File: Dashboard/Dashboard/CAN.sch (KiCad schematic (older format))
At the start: 23 parts, among them J4 CAN_Out, U4 ADM3055E, U5 CDSOT23-T24CAN

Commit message: Make major changes to Dashboard and file structure.
Problem
=======
* The dashboard needs to be redesigned. These are continuing changes
to Dashboard 2.0.
* There are way too many files cluttering the Dashboard folder.
* We need to include LED indicators for the driver that make sense.

Solution
========
* I made major changes to the dashboard. These include the following:
  * Add an external LED board to mount on the steering wheel.
  * Add hardware timer circuitry for lights, so that the software does
    not have to concern itself with the flashers.
  * Generally cleaned up the dashboard's schematics
* There have also been changes made to the file system. All extra files
  that were not necessary have been removed. In the future, reference
  materials should be kept outside of version control.

Notes
=====
The dashboard still is not complete. We still need to address the following:
1. Pin assignments right now are mostly arbitrary. They are still subject to change.
2. The design needs to be verified.
3. We need to settle on the interface. Things like the ignition dial are still
   possible to change if we desire.
4. We need to add another potentiometer for the accelerator. This is missing because
   it was previously handled by the motor interface board.
5. Probably some other things that I'm forgetting.
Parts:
- removed J4: CAN_Out, UTSVT_Connectors:Molex_MicroFit3.0_1x4xP3.00mm_PolarizingPeg_Vertical, symbol utsvt-connectors:CANConnector
- removed TP6: CAN_ISO_Vout, TestPoint:TestPoint_Keystone_5005-5009_Compact, symbol Connector:TestPoint
- removed TP7: CAN_ISO_Vin, TestPoint:TestPoint_Keystone_5005-5009_Compact, symbol Connector:TestPoint
- removed TP8: CAN_ISO_GndIn, TestPoint:TestPoint_Keystone_5005-5009_Compact, symbol Connector:TestPoint
- removed TP9: CAN_ISO_GndOut, TestPoint:TestPoint_Keystone_5005-5009_Compact, symbol Connector:TestPoint
- removed U4: ADM3055E, UTSVT_ICs:SOIC-20W_7.5x15.4mm_Pitch1.27mm, symbol utsvt-chips:ADM3055E
- removed U5: CDSOT23-T24CAN, Package_TO_SOT_SMD:SOT-23W, symbol utsvt-chips:CDSOT23-T24CAN
- added J201: CAN_IN, utsvt_conn:Molex_MicroFit3.0_1x4xP3.00mm_PolarizingPeg_Vertical, symbol Connector_Generic:Conn_01x04
- added J202: CAN_OUT, utsvt_conn:Molex_MicroFit3.0_1x4xP3.00mm_PolarizingPeg_Vertical, symbol Connector_Generic:Conn_01x04
- added U201: ADM3055E, utsvt_ics:SOIC-20W_7.5x15.4mm_Pitch1.27mm, symbol Chips:ADM3055E
- added U202: CDSOT23-T24CAN, Package_TO_SOT_SMD:SOT-23W, symbol Chips:CDSOT23-T24CAN
- C201: renamed from C18; Mouser Part Number (none) -> 80-C0805C106K8RAUTO
- C202: renamed from C19; Mouser Part Number (none) -> 80-C0805C104K3R
- C203: renamed from C20; Mouser Part Number (none) -> 80-C0805C104K3R
- C204: renamed from C21; Mouser Part Number (none) -> 80-C0805X103K1R3316
- C205: renamed from C22; value 10uF -> 0.22uF; Mouser Part Number (none) -> 80-C0805C224J1RECTU
- C206: renamed from C23; value 0.22uF -> 10uF; Mouser Part Number (none) -> 80-C0805C106K8RAUTO
- C207: renamed from C24; Mouser Part Number (none) -> 80-C0805C104K3R
- C208: renamed from C25; Mouser Part Number (none) -> 80-C0805X103K1R3316
- L201: renamed from L2; Mouser Part Number (none) -> 963-BK2125LM182-T
- L202: renamed from L3; Mouser Part Number (none) -> 963-BK2125LM182-T
- R201: renamed from R2; Mouser Part Number (none) -> 71-CRCW08050000Z0EAC
- R202: renamed from R3; Mouser Part Number (none) -> 71-CRCW080559R0FKEA
- R203: renamed from R4; Mouser Part Number (none) -> 71-CRCW080559R0FKEA
- renumbered JP1 to JP201, TP10 to TP201, TP11 to TP202
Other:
- note added: "As long as total equals to 120 Ohms,\nthe two termination resistors can be any value"

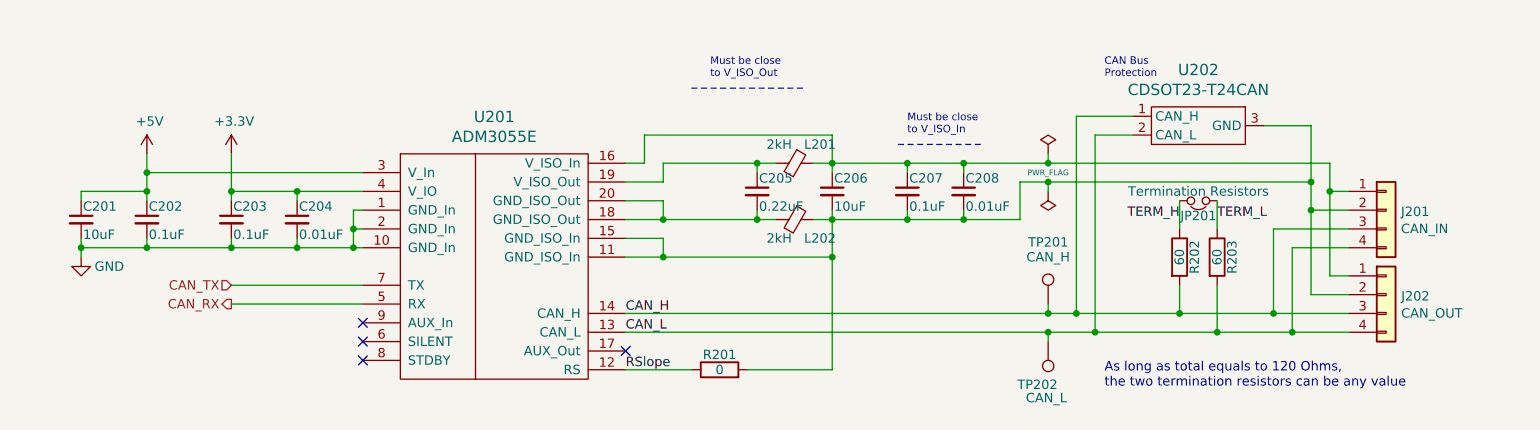
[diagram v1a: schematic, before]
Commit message: Change the MCU to the R (64-pin) variant.
Problem
=======
I don't want to have to solder 144 pins.

Solution
========
I changed the package of the MCU to the 64-pin
version, which now makes it the exact same as
the BPS.
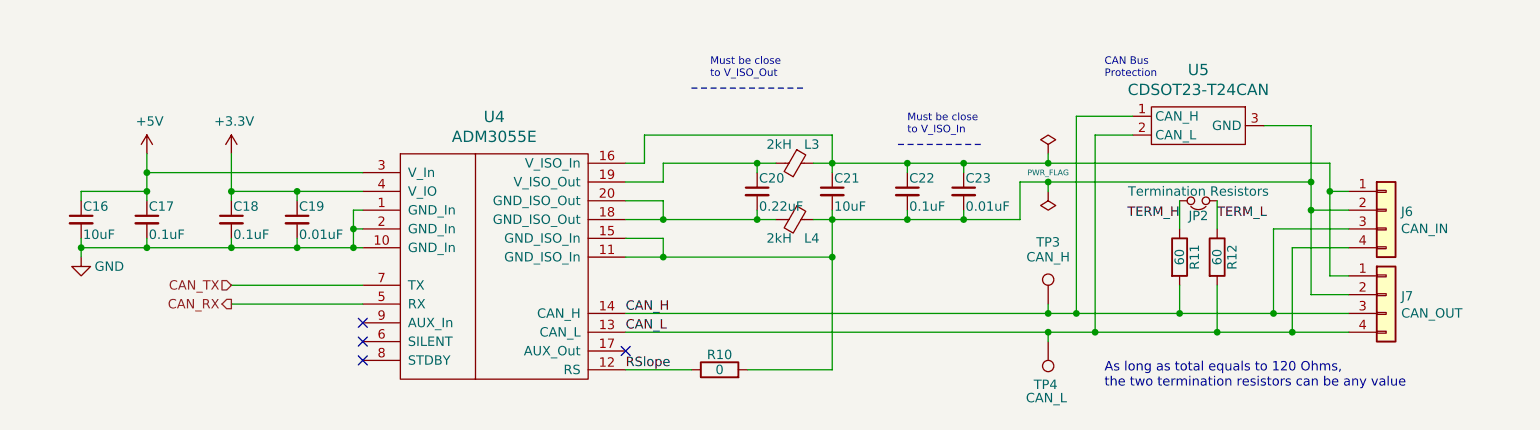
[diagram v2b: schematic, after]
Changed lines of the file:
@@
 $Descr A4 11693 8268
 encoding utf-8
-Sheet 2 6
+Sheet 5 6
 Title ""
 Date ""
@@
 AR Path="/5E80FF20/5C2B42FA" Ref="R?"  Part="1"
 AR Path="/5EA71171/5C2B42FA" Ref="R503"  Part="1"
-F 0 "R203" V 8280 3550 50  0000 C CNN
+AR Path="/5F479052/5C2B42FA" Ref="R9"  Part="1"
+AR Path="/5F547B94/5C2B42FA" Ref="R12"  Part="1"
+F 0 "R12" V 8280 3550 50  0000 C CNN
 F 1 "60" V 8200 3550 50  0000 C CNN
 F 2 "Resistor_SMD:R_0805_2012Metric" V 8130 3550 50  0001 C CNN
@@
 AR Path="/5E80FF20/5C2B4301" Ref="R?"  Part="1"
 AR Path="/5EA71171/5C2B4301" Ref="R502"  Part="1"
-F 0 "R202" V 8080 3550 50  0000 C CNN
+AR Path="/5F479052/5C2B4301" Ref="R8"  Part="1"
+AR Path="/5F547B94/5C2B4301" Ref="R11"  Part="1"
+F 0 "R11" V 8080 3550 50  0000 C CNN
 F 1 "60" V 8000 3550 50  0000 C CNN
 F 2 "Resistor_SMD:R_0805_2012Metric" V 7930 3550 50  0001 C CNN
@@
 AR Path="/5E80FF20/5C2B4308" Ref="JP?"  Part="1"
 AR Path="/5EA71171/5C2B4308" Ref="JP501"  Part="1"
-F 0 "JP201" H 8100 3330 50  0000 C CNN
+AR Path="/5F479052/5C2B4308" Ref="JP1"  Part="1"
+AR Path="/5F547B94/5C2B4308" Ref="JP2"  Part="1"
+F 0 "JP2" H 8100 3330 50  0000 C CNN
 F 1 "Termination Resistors" H 8100 3200 50  0000 C CNN
 F 2 "Connector_PinHeader_2.54mm:PinHeader_1x02_P2.54mm_Vertical" H 8100 3250 50  0001 C CNN
@@
 AR Path="/5E80FF20/5C2B4310" Ref="C?"  Part="1"
 AR Path="/5EA71171/5C2B4310" Ref="C501"  Part="1"
-F 0 "C201" H 2160 3420 50  0000 L CNN
+AR Path="/5F479052/5C2B4310" Ref="C8"  Part="1"
+AR Path="/5F547B94/5C2B4310" Ref="C16"  Part="1"
+F 0 "C16" H 2160 3420 50  0000 L CNN
 F 1 "10uF" H 2160 3270 50  0000 L CNN
 F 2 "Capacitor_SMD:C_0805_2012Metric" H 2150 3350 50  0001 C CNN
@@
 AR Path="/5E80FF20/5C2B4317" Ref="C?"  Part="1"
 AR Path="/5EA71171/5C2B4317" Ref="C502"  Part="1"
-F 0 "C202" H 2510 3420 50  0000 L CNN
+AR Path="/5F479052/5C2B4317" Ref="C9"  Part="1"
+AR Path="/5F547B94/5C2B4317" Ref="C17"  Part="1"
+F 0 "C17" H 2510 3420 50  0000 L CNN
 F 1 "0.1uF" H 2510 3270 50  0000 L CNN
 F 2 "Capacitor_SMD:C_0805_2012Metric" H 2500 3350 50  0001 C CNN
@@
 AR Path="/5E80FF20/5C2B431E" Ref="C?"  Part="1"
 AR Path="/5EA71171/5C2B431E" Ref="C503"  Part="1"
-F 0 "C203" H 2960 3420 50  0000 L CNN
+AR Path="/5F479052/5C2B431E" Ref="C10"  Part="1"
+AR Path="/5F547B94/5C2B431E" Ref="C18"  Part="1"
+F 0 "C18" H 2960 3420 50  0000 L CNN
 F 1 "0.1uF" H 2960 3270 50  0000 L CNN
 F 2 "Capacitor_SMD:C_0805_2012Metric" H 2950 3350 50  0001 C CNN
@@
 AR Path="/5E80FF20/5C2B4325" Ref="C?"  Part="1"
 AR Path="/5EA71171/5C2B4325" Ref="C504"  Part="1"
-F 0 "C204" H 3310 3420 50  0000 L CNN
+AR Path="/5F479052/5C2B4325" Ref="C11"  Part="1"
+AR Path="/5F547B94/5C2B4325" Ref="C19"  Part="1"
+F 0 "C19" H 3310 3420 50  0000 L CNN
 F 1 "0.01uF" H 3310 3270 50  0000 L CNN
 F 2 "Capacitor_SMD:C_0805_2012Metric" H 3300 3350 50  0001 C CNN
@@
 AR Path="/5E80FF20/5C2B432E" Ref="C?"  Part="1"
 AR Path="/5EA71171/5C2B432E" Ref="C506"  Part="1"
-F 0 "C206" H 6160 3270 50  0000 L CNN
+AR Path="/5F479052/5C2B432E" Ref="C13"  Part="1"
+AR Path="/5F547B94/5C2B432E" Ref="C21"  Part="1"
+F 0 "C21" H 6160 3270 50  0000 L CNN
 F 1 "10uF" H 6160 3120 50  0000 L CNN
 F 2 "Capacitor_SMD:C_0805_2012Metric" H 6150 3200 50  0001 C CNN
@@
 AR Path="/5E80FF20/5C2B4335" Ref="C?"  Part="1"
 AR Path="/5EA71171/5C2B4335" Ref="C505"  Part="1"
-F 0 "C205" H 5760 3270 50  0000 L CNN
+AR Path="/5F479052/5C2B4335" Ref="C12"  Part="1"
+AR Path="/5F547B94/5C2B4335" Ref="C20"  Part="1"
+F 0 "C20" H 5760 3270 50  0000 L CNN
 F 1 "0.22uF" H 5760 3120 50  0000 L CNN
 F 2 "Capacitor_SMD:C_0805_2012Metric" H 5750 3200 50  0001 C CNN
@@
 AR Path="/5E80FF20/5C2B433C" Ref="L?"  Part="1"
 AR Path="/5EA71171/5C2B433C" Ref="L501"  Part="1"
-F 0 "L201" V 5850 3100 50  0000 L CNN
+AR Path="/5F479052/5C2B433C" Ref="L1"  Part="1"
+AR Path="/5F547B94/5C2B433C" Ref="L3"  Part="1"
+F 0 "L3" V 5850 3100 50  0000 L CNN
 F 1 "2kH" V 5850 2900 50  0000 L CNN
 F 2 "Inductor_SMD:L_0805_2012Metric" V 5880 3050 50  0001 C CNN
@@
 AR Path="/5E80FF20/5C2B4343" Ref="L?"  Part="1"
 AR Path="/5EA71171/5C2B4343" Ref="L502"  Part="1"
-F 0 "L202" V 6050 3400 50  0000 L CNN
+AR Path="/5F479052/5C2B4343" Ref="L2"  Part="1"
+AR Path="/5F547B94/5C2B4343" Ref="L4"  Part="1"
+F 0 "L4" V 6050 3400 50  0000 L CNN
 F 1 "2kH" V 6050 3200 50  0000 L CNN
 F 2 "Inductor_SMD:L_0805_2012Metric" V 5880 3350 50  0001 C CNN
@@
 AR Path="/5E80FF20/5C2B434A" Ref="C?"  Part="1"
 AR Path="/5EA71171/5C2B434A" Ref="C507"  Part="1"
-F 0 "C207" H 6560 3270 50  0000 L CNN
+AR Path="/5F479052/5C2B434A" Ref="C14"  Part="1"
+AR Path="/5F547B94/5C2B434A" Ref="C22"  Part="1"
+F 0 "C22" H 6560 3270 50  0000 L CNN
 F 1 "0.1uF" H 6560 3120 50  0000 L CNN
 F 2 "Capacitor_SMD:C_0805_2012Metric" H 6550 3200 50  0001 C CNN
@@
 AR Path="/5E80FF20/5C2B4351" Ref="C?"  Part="1"
 AR Path="/5EA71171/5C2B4351" Ref="C508"  Part="1"
-F 0 "C208" H 6860 3270 50  0000 L CNN
+AR Path="/5F479052/5C2B4351" Ref="C15"  Part="1"
+AR Path="/5F547B94/5C2B4351" Ref="C23"  Part="1"
+F 0 "C23" H 6860 3270 50  0000 L CNN
 F 1 "0.01uF" H 6860 3120 50  0000 L CNN
 F 2 "Capacitor_SMD:C_0805_2012Metric" H 6850 3200 50  0001 C CNN
@@
 AR Path="/5E80FF20/5C2B4394" Ref="#FLG?"  Part="1"
 AR Path="/5EA71171/5C2B4394" Ref="#FLG0501"  Part="1"
-F 0 "#FLG0201" H 7300 3075 50  0001 C CNN
+AR Path="/5F479052/5C2B4394" Ref="#FLG0101"  Part="1"
+AR Path="/5F547B94/5C2B4394" Ref="#FLG0103"  Part="1"
+F 0 "#FLG0103" H 7300 3075 50  0001 C CNN
 F 1 "PWR_FLAG" H 7300 2900 30  0000 C CNN
 F 2 "" H 7300 3000 50  0001 C CNN
@@
 AR Path="/5E80FF20/5C2B439A" Ref="#FLG?"  Part="1"
 AR Path="/5EA71171/5C2B439A" Ref="#FLG0502"  Part="1"
-F 0 "#FLG0202" H 7300 3275 50  0001 C CNN
+AR Path="/5F479052/5C2B439A" Ref="#FLG0102"  Part="1"
+AR Path="/5F547B94/5C2B439A" Ref="#FLG0104"  Part="1"
+F 0 "#FLG0104" H 7300 3275 50  0001 C CNN
 F 1 "PWR_FLAG" H 7200 3150 50  0001 L CNN
 F 2 "" H 7300 3200 50  0001 C CNN
@@
 AR Path="/5E80FF20/5C2B43B6" Ref="TP?"  Part="1"
 AR Path="/5EA71171/5C2B43B6" Ref="TP501"  Part="1"
-F 0 "TP201" H 7300 4100 50  0000 C BNN
+AR Path="/5F479052/5C2B43B6" Ref="TP1"  Part="1"
+AR Path="/5F547B94/5C2B43B6" Ref="TP3"  Part="1"
+F 0 "TP3" H 7300 4100 50  0000 C BNN
 F 1 "CAN_H" H 7300 4050 50  0000 C CNN
 F 2 "TestPoint:TestPoint_Keystone_5005-5009_Compact" H 7300 3800 50  0001 C CNN
@@
 AR Path="/5E80FF20/5C2B43BD" Ref="TP?"  Part="1"
 AR Path="/5EA71171/5C2B43BD" Ref="TP502"  Part="1"
-F 0 "TP202" H 7250 4200 50  0000 L BNN
+AR Path="/5F479052/5C2B43BD" Ref="TP2"  Part="1"
+AR Path="/5F547B94/5C2B43BD" Ref="TP4"  Part="1"
+F 0 "TP4" H 7250 4200 50  0000 L BNN
 F 1 "CAN_L" H 7200 4300 50  0000 L CNN
 F 2 "TestPoint:TestPoint_Keystone_5005-5009_Compact" H 7300 4000 50  0001 C CNN
@@
 AR Path="/5E80FF20/5C2B43C4" Ref="R?"  Part="1"
 AR Path="/5EA71171/5C2B43C4" Ref="R501"  Part="1"
-F 0 "R201" V 5630 4150 50  0000 C CNN
+AR Path="/5F479052/5C2B43C4" Ref="R7"  Part="1"
+AR Path="/5F547B94/5C2B43C4" Ref="R10"  Part="1"
+F 0 "R10" V 5630 4150 50  0000 C CNN
 F 1 "0" V 5550 4150 50  0000 C CNN
 F 2 "Resistor_SMD:R_0805_2012Metric" V 5480 4150 50  0001 C CNN
@@
 AR Path="/5E80FF20/5C28BDDE" Ref="#PWR?"  Part="1"
 AR Path="/5EA71171/5C28BDDE" Ref="#PWR0501"  Part="1"
-F 0 "#PWR0201" H 2150 3300 50  0001 C CNN
+AR Path="/5F479052/5C28BDDE" Ref="#PWR0158"  Part="1"
+AR Path="/5F547B94/5C28BDDE" Ref="#PWR0176"  Part="1"
+F 0 "#PWR0176" H 2150 3300 50  0001 C CNN
 F 1 "GND" H 2300 3500 50  0000 C CNN
 F 2 "" H 2150 3550 50  0001 C CNN
@@
 AR Path="/5E80FF20/5C4ABE05" Ref="#PWR?"  Part="1"
 AR Path="/5EA71171/5C4ABE05" Ref="#PWR0503"  Part="1"
-F 0 "#PWR0203" H 2950 2850 50  0001 C CNN
+AR Path="/5F479052/5C4ABE05" Ref="#PWR0159"  Part="1"
+AR Path="/5F547B94/5C4ABE05" Ref="#PWR0186"  Part="1"
+F 0 "#PWR0186" H 2950 2850 50  0001 C CNN
 F 1 "+3.3V" H 2965 3173 50  0000 C CNN
 F 2 "" H 2950 3000 50  0001 C CNN
@@
 AR Path="/5E80FF20/5C4C2AB0" Ref="#PWR?"  Part="1"
 AR Path="/5EA71171/5C4C2AB0" Ref="#PWR0502"  Part="1"
-F 0 "#PWR0202" H 2500 2850 50  0001 C CNN
+AR Path="/5F479052/5C4C2AB0" Ref="#PWR0160"  Part="1"
+AR Path="/5F547B94/5C4C2AB0" Ref="#PWR0187"  Part="1"
+F 0 "#PWR0187" H 2500 2850 50  0001 C CNN
 F 1 "+5V" H 2515 3173 50  0000 C CNN
 F 2 "" H 2500 3000 50  0001 C CNN
@@
 AR Path="/5E80FF20/5F15D99A" Ref="J?"  Part="1"
 AR Path="/5EA71171/5F15D99A" Ref="J502"  Part="1"
-F 0 "J202" H 9180 3742 50  0000 L CNN
+AR Path="/5F479052/5F15D99A" Ref="J5"  Part="1"
+AR Path="/5F547B94/5F15D99A" Ref="J7"  Part="1"
+F 0 "J7" H 9180 3742 50  0000 L CNN
 F 1 "CAN_OUT" H 9180 3651 50  0000 L CNN
 F 2 "utsvt_conn:Molex_MicroFit3.0_1x4xP3.00mm_PolarizingPeg_Vertical" H 9100 3750 50  0001 C CNN
@@
 AR Path="/5E80FF20/5F175F7A" Ref="U?"  Part="1"
 AR Path="/5EA71171/5F175F7A" Ref="U501"  Part="1"
-F 0 "U201" H 4350 4397 60  0000 C CNN
+AR Path="/5F479052/5F175F7A" Ref="U2"  Part="1"
+AR Path="/5F547B94/5F175F7A" Ref="U4"  Part="1"
+F 0 "U4" H 4350 4397 60  0000 C CNN
 F 1 "ADM3055E" H 4350 4291 60  0000 C CNN
 F 2 "utsvt_ics:SOIC-20W_7.5x15.4mm_Pitch1.27mm" H 4350 3700 60  0001 C CNN
@@
 AR Path="/5E80FF20/5F177CC0" Ref="U?"  Part="1"
 AR Path="/5EA71171/5F177CC0" Ref="U502"  Part="1"
-F 0 "U202" H 8100 3147 60  0000 C CNN
+AR Path="/5F479052/5F177CC0" Ref="U3"  Part="1"
+AR Path="/5F547B94/5F177CC0" Ref="U5"  Part="1"
+F 0 "U5" H 8100 3147 60  0000 C CNN
 F 1 "CDSOT23-T24CAN" H 8100 3041 60  0000 C CNN
 F 2 "Package_TO_SOT_SMD:SOT-23W" H 8100 2850 60  0001 C CNN
@@
 AR Path="/5E5E1F90/5E667EFE" Ref="J201"  Part="1"
 AR Path="/5EA71171/5E667EFE" Ref="J501"  Part="1"
-F 0 "J201" H 9179 3292 50  0000 L CNN
+AR Path="/5F479052/5E667EFE" Ref="J4"  Part="1"
+AR Path="/5F547B94/5E667EFE" Ref="J6"  Part="1"
+F 0 "J6" H 9179 3292 50  0000 L CNN
 F 1 "CAN_IN" H 9179 3201 50  0000 L CNN
 F 2 "utsvt_conn:Molex_MicroFit3.0_1x4xP3.00mm_PolarizingPeg_Vertical" H 9100 3300 50  0001 C CNN

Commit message: Add redundant potentiometers and relabel components.
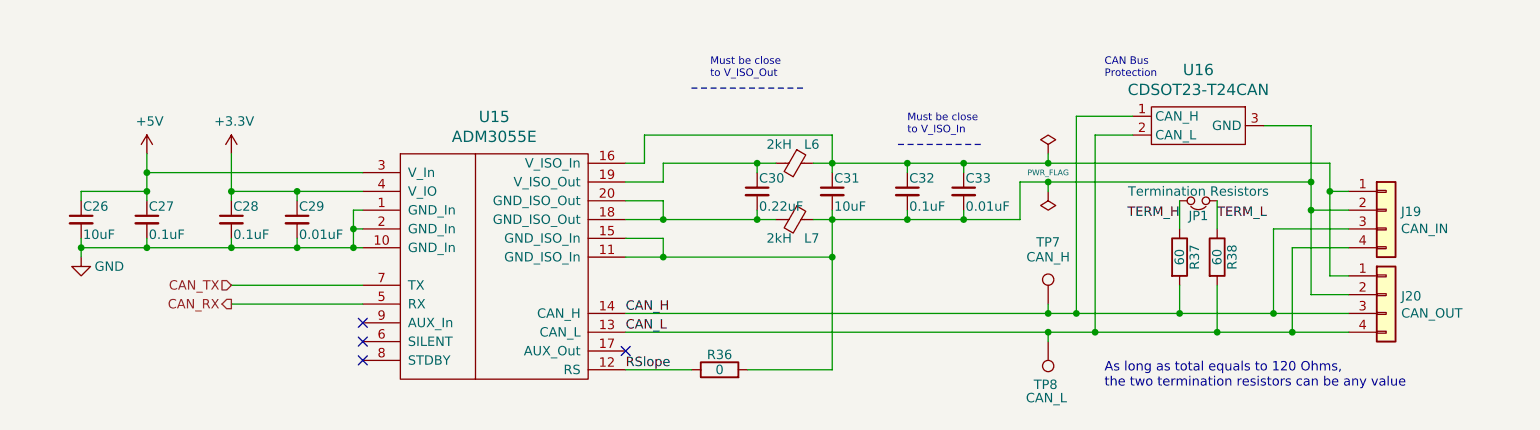
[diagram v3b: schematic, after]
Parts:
- renumbered C201 to C26, C202 to C27, C203 to C28, C204 to C29, C205 to C30, C206 to C31, C207 to C32, C208 to C33, J201 to J19, J202 to J20, JP201 to JP1, L201 to L6, L202 to L7, R201 to R36, R202 to R37, R203 to R38, TP201 to TP7, TP202 to TP8, U201 to U15, U202 to U16
